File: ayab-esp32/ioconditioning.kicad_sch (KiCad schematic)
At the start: 29 parts, among them U702 LM393, U703 LM393

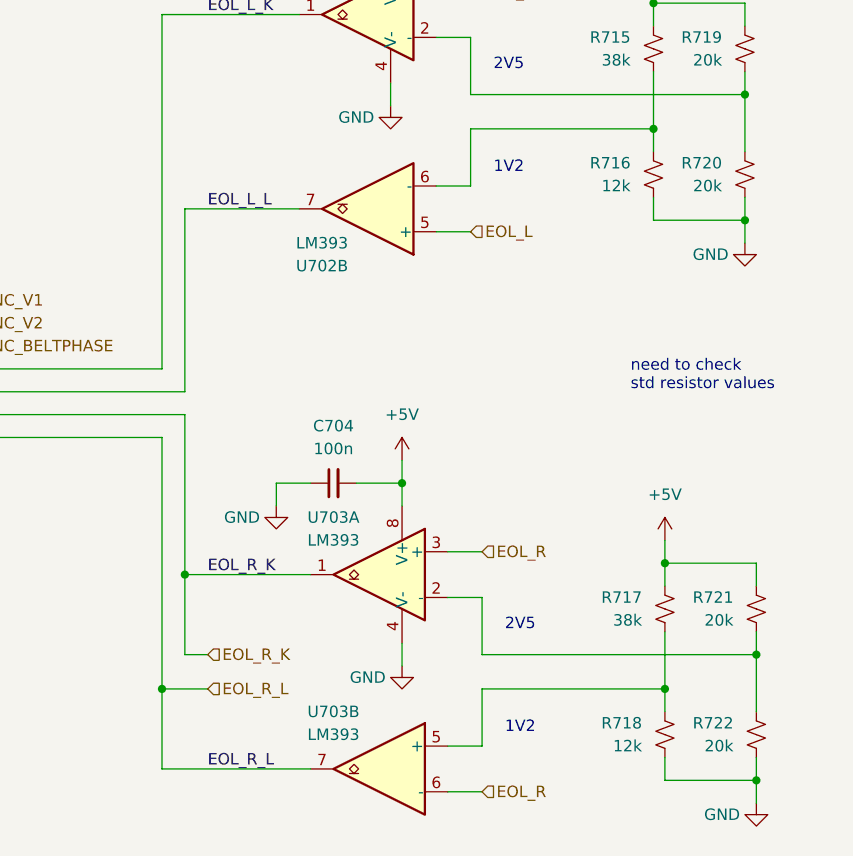
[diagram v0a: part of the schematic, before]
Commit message: fix comparator
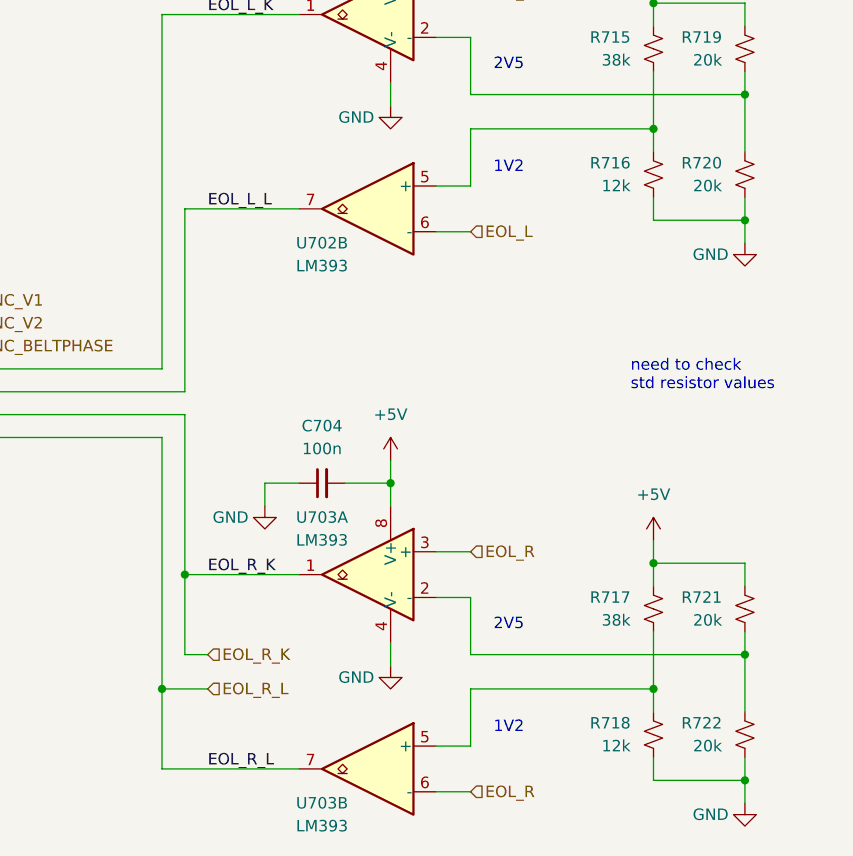
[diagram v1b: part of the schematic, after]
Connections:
- net EOL_L: now also U702.6 (-); no longer U702.5 (+)
- net at R715.2, R716.1: now also U702.5 (+); no longer U702.6 (-)
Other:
- company: (none) -> matei
- title: (none) -> I/O CONDITIONING
- moved on the sheet: C704, R717, R718, R721, R722, U702B, U703A, U703B

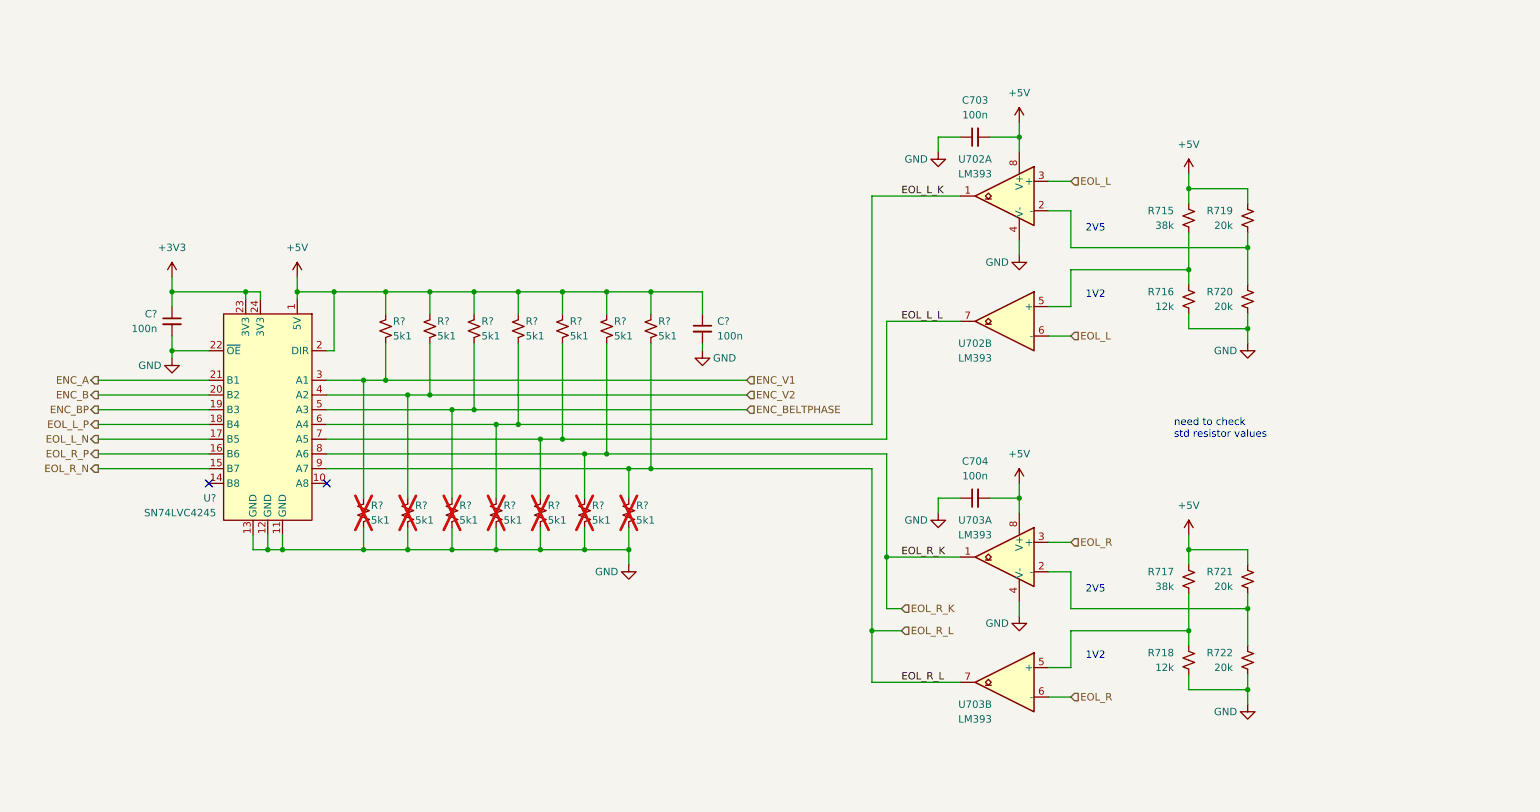
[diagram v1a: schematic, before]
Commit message: fix folder structure and update gitignore
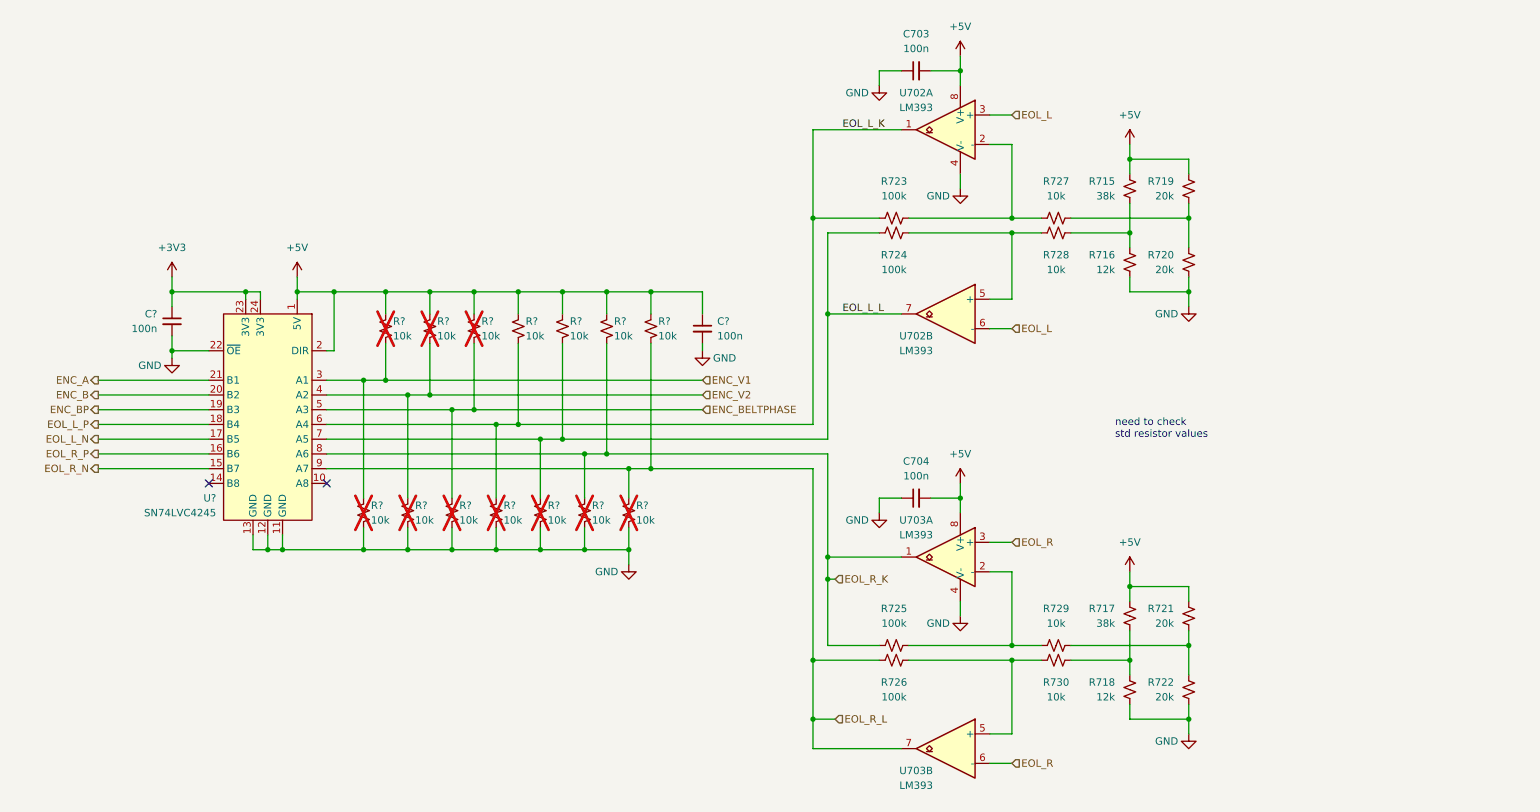
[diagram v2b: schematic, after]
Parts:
- added R723, R724, R725, R726: 100k, symbol ayab-esp32:R_Small_US
- added R727, R728, R729, R730: 10k, symbol ayab-esp32:R_Small_US
- C703, C704, C? (x2): symbol Device:C_Small -> ayab-esp32:C_Small
- R715, R716, R717, R718, R719, R720, R721, R722: symbol Device:R_Small_US -> ayab-esp32:R_Small_US
- R? (x11): value 5k1 -> 10k; symbol Device:R_Small_US -> ayab-esp32:R_Small_US
- R? (x3): value 5k1 -> 10k; symbol Device:R_Small_US -> ayab-esp32:R_Small_US; now not fitted; now left out of the parts list
- U702, U703: symbol Comparator:LM393 -> ayab-esp32:LM393
- U?: symbol matei:SN74LVC4245A -> ayab-esp32:SN74LVC4245A
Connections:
- net EOL_L_K: now also R723.1
- net EOL_L_L: now also R724.2
- net EOL_R_K: now also R725.1
- net EOL_R_L: now also R726.2
- net at R719.2, R720.1: now also R727.2; no longer U702.2 (-)
- net at R721.2, R722.1: now also R729.2; no longer U703.2 (-)
- net at R715.2, R716.1: now also R728.1; no longer U702.5 (+)
- net at R717.2, R718.1: now also R730.1; no longer U703.5 (+)
- new net: R726.1, R730.2, U703.5 (+)
- new net: R725.2, R729.1, U703.2 (-)
- new net: R723.2, R727.1, U702.2 (-)
- new net: R724.1, R728.2, U702.5 (+)
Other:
- note removed: "1V2"
- note removed: "2V5"
- moved on the sheet: C703, C704, R715, R716, R717, R718, R719, R720, R721, R722, U702A, U702B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

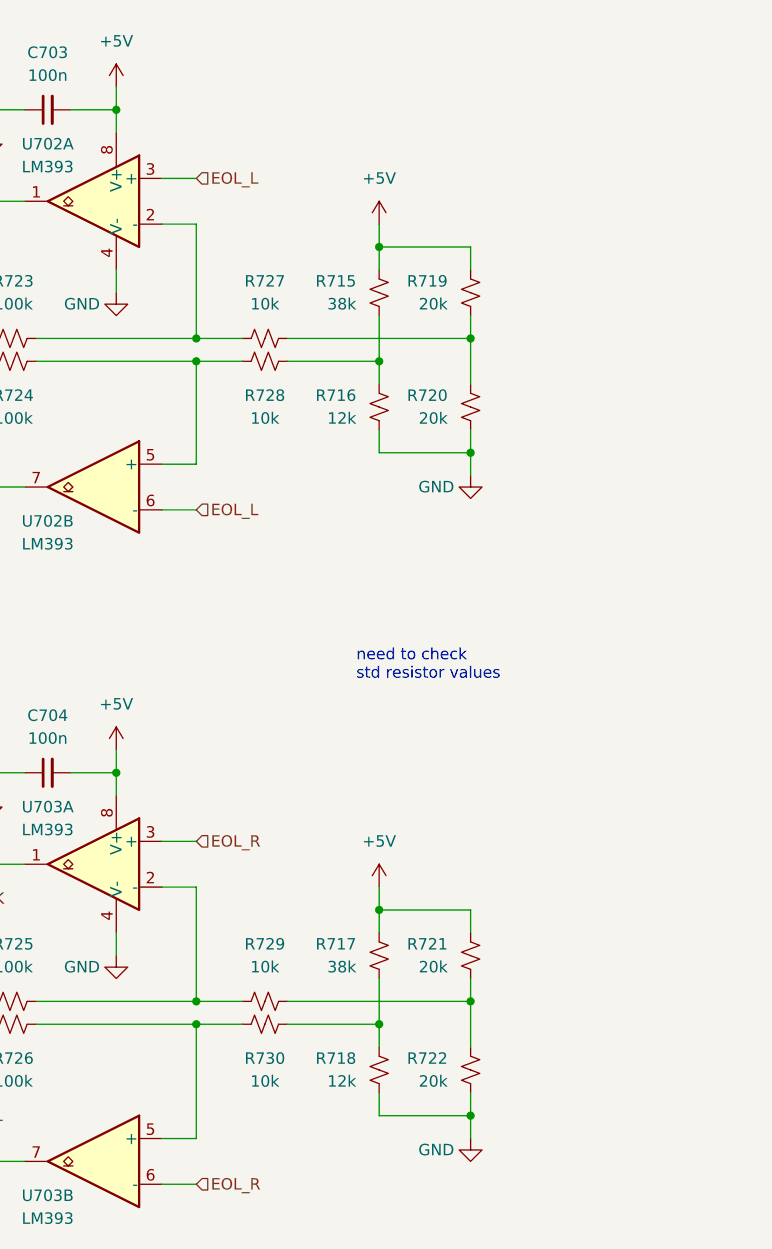
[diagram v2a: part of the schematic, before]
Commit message: comparator biasing and cleanup
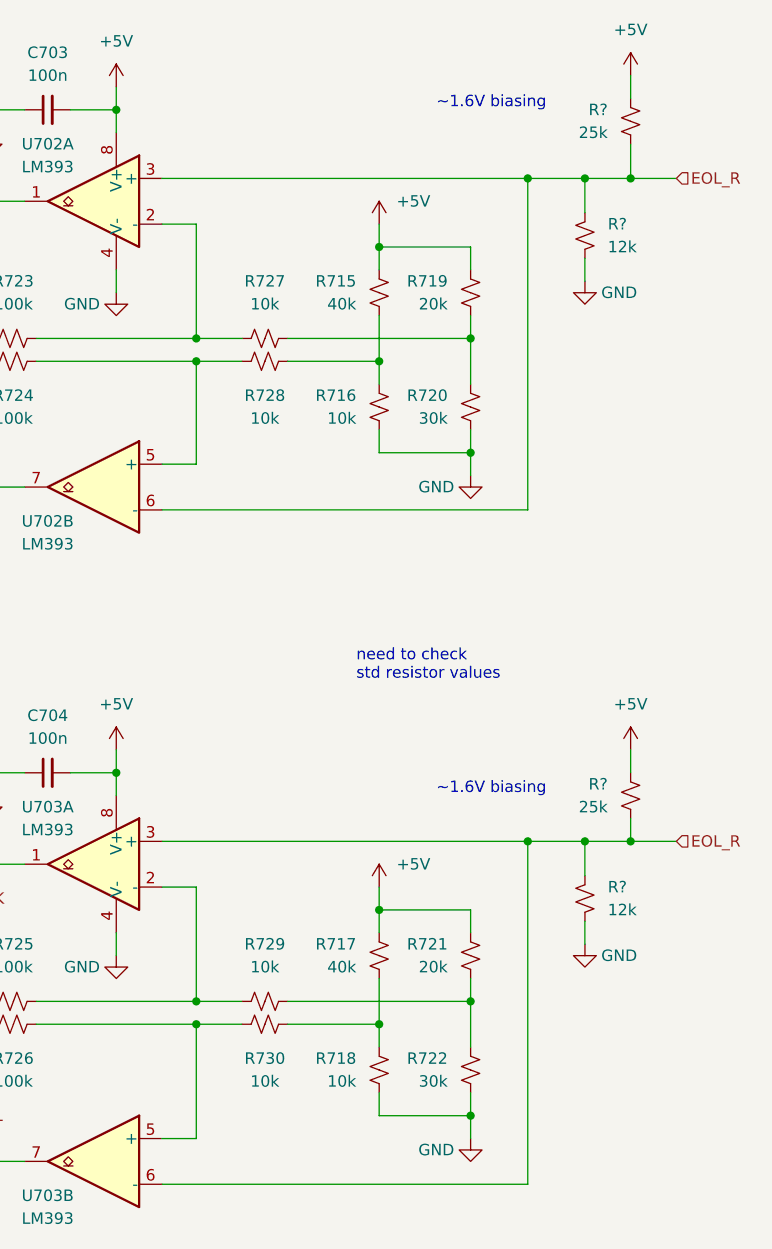
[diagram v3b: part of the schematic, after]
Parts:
- added R? (x2): 25k, symbol ayab-esp32:R_Small_US
- added R? (x2): 12k, symbol ayab-esp32:R_Small_US
- R715, R717: value 38k -> 40k
- R716, R718: value 12k -> 10k
- R720, R722: value 20k -> 30k
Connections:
- net EOL_L is gone; now on net EOL_R: U702.3 (+), U702.6 (-)
- net +5V: now also R?.1, R?.1
- net EOL_R: now also R?.1, R?.1, R?.2, R?.2
- net GND: now also R?.2, R?.2
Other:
- note added: "~1.6V biasing"

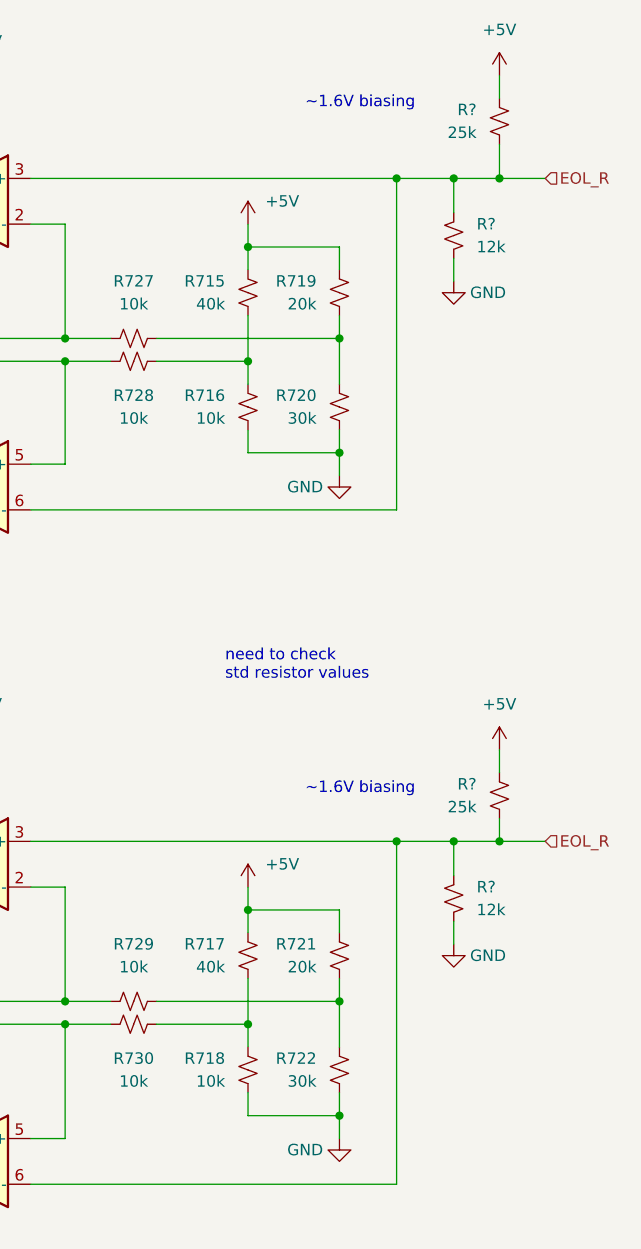
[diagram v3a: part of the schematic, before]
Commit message: fix comparator bias and hysteresis
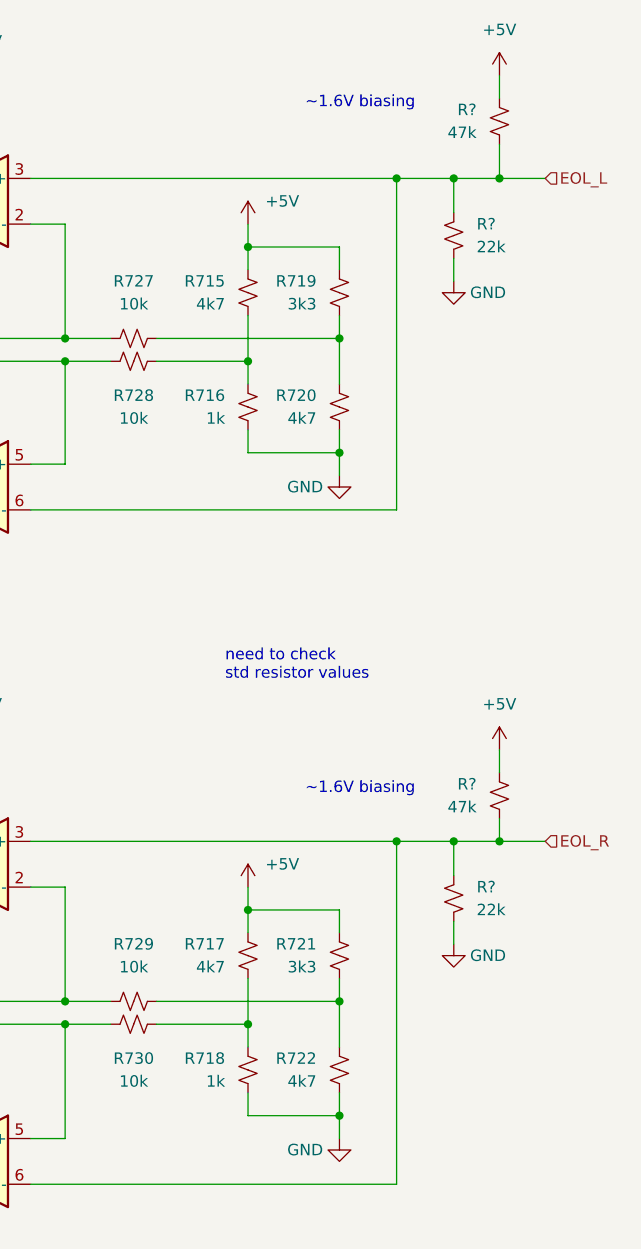
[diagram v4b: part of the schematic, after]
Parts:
- R715, R717: value 40k -> 4k7
- R716, R718: value 10k -> 1k
- R719, R721: value 20k -> 3k3
- R720, R722: value 30k -> 4k7
- R? (x2): value 25k -> 47k
- R? (x2): value 12k -> 22k
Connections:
- net EOL_R: no longer R?.1, R?.2, U702.3 (+), U702.6 (-)
- new net EOL_L: R?.1, R?.2, U702.3 (+), U702.6 (-)
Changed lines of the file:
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@@
     (effects (font (size 1.27 1.27)) (justify left bottom))
   )
-  (hierarchical_label "EOL_R" (shape input) (at 248.92 39.37 0) (fields_autoplaced)
+  (hierarchical_label "EOL_L" (shape input) (at 248.92 39.37 0) (fields_autoplaced)
     (effects (font (size 1.27 1.27)) (justify left))
   )
@@
       (effects (font (size 1.27 1.27)) (justify right))
     )
-    (property "Value" "30k" (at 223.52 66.04 0)
+    (property "Value" "4k7" (at 223.52 66.04 0)
       (effects (font (size 1.27 1.27)) (justify right))
     )
@@
       (effects (font (size 1.27 1.27)) (justify right))
     )
-    (property "Value" "30k" (at 223.52 139.7 0)
+    (property "Value" "4k7" (at 223.52 139.7 0)
       (effects (font (size 1.27 1.27)) (justify right))
     )
@@
       (effects (font (size 1.27 1.27)) (justify right))
     )
-    (property "Value" "20k" (at 223.52 53.34 0)
+    (property "Value" "3k3" (at 223.52 53.34 0)
       (effects (font (size 1.27 1.27)) (justify right))
     )
@@
       (effects (font (size 1.27 1.27)) (justify right))
     )
-    (property "Value" "25k" (at 241.3 109.22 0)
+    (property "Value" "47k" (at 241.3 109.22 0)
       (effects (font (size 1.27 1.27)) (justify right))
     )
@@
       (effects (font (size 1.27 1.27)) (justify right))
     )
-    (property "Value" "10k" (at 213.36 139.7 0)
+    (property "Value" "1k" (at 213.36 139.7 0)
       (effects (font (size 1.27 1.27)) (justify right))
     )
@@
       (effects (font (size 1.27 1.27)) (justify right))
     )
-    (property "Value" "25k" (at 241.3 34.29 0)
+    (property "Value" "47k" (at 241.3 34.29 0)
       (effects (font (size 1.27 1.27)) (justify right))
     )
@@
       (effects (font (size 1.27 1.27)) (justify right))
     )
-    (property "Value" "20k" (at 223.52 127 0)
+    (property "Value" "3k3" (at 223.52 127 0)
       (effects (font (size 1.27 1.27)) (justify right))
     )
@@
       (effects (font (size 1.27 1.27)) (justify right))
     )
-    (property "Value" "40k" (at 213.36 127 0)
+    (property "Value" "4k7" (at 213.36 127 0)
       (effects (font (size 1.27 1.27)) (justify right))
     )
@@
       (effects (font (size 1.27 1.27)) (justify right))
     )
-    (property "Value" "12k" (at 241.3 120.65 0)
+    (property "Value" "22k" (at 241.3 120.65 0)
       (effects (font (size 1.27 1.27)) (justify right))
     )
@@
       (effects (font (size 1.27 1.27)) (justify right))
     )
-    (property "Value" "10k" (at 213.36 66.04 0)
+    (property "Value" "1k" (at 213.36 66.04 0)
       (effects (font (size 1.27 1.27)) (justify right))
     )
@@
       (effects (font (size 1.27 1.27)) (justify right))
     )
-    (property "Value" "40k" (at 213.36 53.34 0)
+    (property "Value" "4k7" (at 213.36 53.34 0)
       (effects (font (size 1.27 1.27)) (justify right))
     )
@@
       (effects (font (size 1.27 1.27)) (justify right))
     )
-    (property "Value" "12k" (at 241.3 46.99 0)
-      (effects (font (size 1.27 1.27)) (justify right))
-    )
+    (property "Value" "22k" (at 241.3 46.99 0)
+      (effects (font (size 1.27 1.27)) (justify right))
+    )
